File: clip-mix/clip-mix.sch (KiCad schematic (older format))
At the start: 22 parts, among them J1 Conn_01x01_Female, J2 Conn_01x01_Female, J3 Conn_01x01_Female, J4 Conn_02x05_Odd_Even, U1 TL074

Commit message: work on test and clip mix
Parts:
- added unit 4 of U1
- C1, C2: value CP1 -> 10uF
- C3, C4: value C -> 0.1uF
- D1, D2: value D -> 1N4148
- D3: value D_Schottky -> 1N5189
- D4: value D_Schottky -> 1N1589
- J1: value Conn_01x01_Female -> IN
- J2: value Conn_01x01_Female -> OUT
- J3: value Conn_01x01_Female -> CLIP OUT
- J4: value Conn_02x05_Odd_Even -> Power
- R1, R2, R3, R4, R7: value R -> 100K
- R5, R8: value R -> 1K
- R6: value R -> 27K
- RV1: value R_POT -> 20K
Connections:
- net -12V: now reaches D4.1 (K), J4.10 (Pin_10), J4.9 (Pin_9)
- net +12v: now reaches D3.2 (A), J4.1 (Pin_1), J4.2 (Pin_2)
- new net: U1.12 (+), U1.13 (-)
- no-connect marks 0 -> 1
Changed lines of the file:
@@
 P 4400 2450
 F 0 "R2" V 4193 2450 50  0000 C CNN
-F 1 "R" V 4284 2450 50  0000 C CNN
+F 1 "100K" V 4284 2450 50  0000 C CNN
 F 2 "Resistor_THT:R_Axial_DIN0204_L3.6mm_D1.6mm_P7.62mm_Horizontal" V 4330 2450 50  0001 C CNN
 F 3 "~" H 4400 2450 50  0001 C CNN
@@
 P 5100 2000
 F 0 "R3" V 4893 2000 50  0000 C CNN
-F 1 "R" V 4984 2000 50  0000 C CNN
+F 1 "100K" V 4984 2000 50  0000 C CNN
 F 2 "Resistor_THT:R_Axial_DIN0204_L3.6mm_D1.6mm_P7.62mm_Horizontal" V 5030 2000 50  0001 C CNN
 F 3 "~" H 5100 2000 50  0001 C CNN
@@
 P 6600 2550
 F 0 "J2" H 6628 2576 50  0000 L CNN
-F 1 "Conn_01x01_Female" H 6628 2485 50  0000 L CNN
+F 1 "OUT" H 6628 2485 50  0000 L CNN
 F 2 "Connector_Wire:SolderWire-0.5sqmm_1x01_D0.9mm_OD2.3mm" H 6600 2550 50  0001 C CNN
 F 3 "~" H 6600 2550 50  0001 C CNN
@@
 P 7900 3350
 F 0 "J3" H 7928 3376 50  0000 L CNN
-F 1 "Conn_01x01_Female" H 7928 3285 50  0000 L CNN
+F 1 "CLIP OUT" H 7928 3285 50  0000 L CNN
 F 2 "Connector_Wire:SolderWire-0.5sqmm_1x01_D0.9mm_OD2.3mm" H 7900 3350 50  0001 C CNN
 F 3 "~" H 7900 3350 50  0001 C CNN
@@
 P 3750 1900
 F 0 "R1" V 3543 1900 50  0000 C CNN
-F 1 "R" V 3634 1900 50  0000 C CNN
+F 1 "100K" V 3634 1900 50  0000 C CNN
 F 2 "Resistor_THT:R_Axial_DIN0204_L3.6mm_D1.6mm_P7.62mm_Horizontal" V 3680 1900 50  0001 C CNN
 F 3 "~" H 3750 1900 50  0001 C CNN
@@
 P 7350 3350
 F 0 "R8" V 7143 3350 50  0000 C CNN
-F 1 "R" V 7234 3350 50  0000 C CNN
+F 1 "1K" V 7234 3350 50  0000 C CNN
 F 2 "Resistor_THT:R_Axial_DIN0204_L3.6mm_D1.6mm_P7.62mm_Horizontal" V 7280 3350 50  0001 C CNN
 F 3 "~" H 7350 3350 50  0001 C CNN
@@
 P 5950 2550
 F 0 "R5" V 5743 2550 50  0000 C CNN
-F 1 "R" V 5834 2550 50  0000 C CNN
+F 1 "1K" V 5834 2550 50  0000 C CNN
 F 2 "Resistor_THT:R_Axial_DIN0204_L3.6mm_D1.6mm_P7.62mm_Horizontal" V 5880 2550 50  0001 C CNN
 F 3 "~" H 5950 2550 50  0001 C CNN
@@
 P 5500 3250
 F 0 "R4" V 5293 3250 50  0000 C CNN
-F 1 "R" V 5384 3250 50  0000 C CNN
+F 1 "100K" V 5384 3250 50  0000 C CNN
 F 2 "Resistor_THT:R_Axial_DIN0204_L3.6mm_D1.6mm_P7.62mm_Horizontal" V 5430 3250 50  0001 C CNN
 F 3 "~" H 5500 3250 50  0001 C CNN
@@
 P 6000 3550
 F 0 "D2" V 5954 3630 50  0000 L CNN
-F 1 "D" V 6045 3630 50  0000 L CNN
+F 1 "1N4148" V 6045 3630 50  0000 L CNN
 F 2 "Diode_THT:D_T-1_P5.08mm_Horizontal" H 6000 3550 50  0001 C CNN
 F 3 "~" H 6000 3550 50  0001 C CNN
@@
 P 5900 3950
 F 0 "RV1" H 5830 3904 50  0000 R CNN
-F 1 "R_POT" H 5830 3995 50  0000 R CNN
+F 1 "20K" H 5830 3995 50  0000 R CNN
 F 2 "Potentiometer_THT:Potentiometer_Bourns_3296W_Vertical" H 5900 3950 50  0001 C CNN
 F 3 "~" H 5900 3950 50  0001 C CNN
@@
 P 5800 3550
 F 0 "D1" V 5846 3470 50  0000 R CNN
-F 1 "D" V 5755 3470 50  0000 R CNN
+F 1 "1N4148" V 5755 3470 50  0000 R CNN
 F 2 "Diode_THT:D_T-1_P5.08mm_Horizontal" H 5800 3550 50  0001 C CNN
 F 3 "~" H 5800 3550 50  0001 C CNN
@@
 P 6700 3750
 F 0 "R7" V 6493 3750 50  0000 C CNN
-F 1 "R" V 6584 3750 50  0000 C CNN
+F 1 "100K" V 6584 3750 50  0000 C CNN
 F 2 "Resistor_THT:R_Axial_DIN0204_L3.6mm_D1.6mm_P7.62mm_Horizontal" V 6630 3750 50  0001 C CNN
 F 3 "~" H 6700 3750 50  0001 C CNN
@@
 P 6350 3950
 F 0 "R6" H 6280 3904 50  0000 R CNN
-F 1 "R" H 6280 3995 50  0000 R CNN
+F 1 "27K" H 6280 3995 50  0000 R CNN
 F 2 "Resistor_THT:R_Axial_DIN0204_L3.6mm_D1.6mm_P7.62mm_Horizontal" V 6280 3950 50  0001 C CNN
 F 3 "~" H 6350 3950 50  0001 C CNN
@@
 P 2500 2350
 F 0 "J1" H 2392 2125 50  0000 C CNN
-F 1 "Conn_01x01_Female" H 2392 2216 50  0000 C CNN
+F 1 "IN" H 2392 2216 50  0000 C CNN
 F 2 "Connector_Wire:SolderWire-0.5sqmm_1x01_D0.9mm_OD2.3mm" H 2500 2350 50  0001 C CNN
 F 3 "~" H 2500 2350 50  0001 C CNN
@@
 P 3100 5550
 F 0 "C3" H 3215 5596 50  0000 L CNN
-F 1 "C" H 3215 5505 50  0000 L CNN
+F 1 "0.1uF" H 3215 5505 50  0000 L CNN
 F 2 "Capacitor_THT:C_Disc_D7.5mm_W5.0mm_P7.50mm" H 3138 5400 50  0001 C CNN
 F 3 "~" H 3100 5550 50  0001 C CNN
@@
 P 2750 5550
 F 0 "C1" H 2865 5596 50  0000 L CNN
-F 1 "CP1" H 2865 5505 50  0000 L CNN
+F 1 "10uF" H 2865 5505 50  0000 L CNN
 F 2 "Capacitor_THT:CP_Radial_D5.0mm_P2.00mm" H 2750 5550 50  0001 C CNN
 F 3 "~" H 2750 5550 50  0001 C CNN
@@
 P 2300 6250
 F 0 "D4" H 2300 6467 50  0000 C CNN
-F 1 "D_Schottky" H 2300 6376 50  0000 C CNN
+F 1 "1N1589" H 2300 6376 50  0000 C CNN
 F 2 "Diode_THT:D_T-1_P5.08mm_Horizontal" H 2300 6250 50  0001 C CNN
 F 3 "~" H 2300 6250 50  0001 C CNN
@@
 P 2300 5350
 F 0 "D3" H 2300 5133 50  0000 C CNN
-F 1 "D_Schottky" H 2300 5224 50  0000 C CNN
+F 1 "1N5189" H 2300 5224 50  0000 C CNN
 F 2 "Diode_THT:D_T-1_P5.08mm_Horizontal" H 2300 5350 50  0001 C CNN
 F 3 "~" H 2300 5350 50  0001 C CNN
@@
 P 2750 6050
 F 0 "C2" H 2635 6004 50  0000 R CNN
-F 1 "CP1" H 2635 6095 50  0000 R CNN
+F 1 "10uF" H 2635 6095 50  0000 R CNN
 F 2 "Capacitor_THT:CP_Radial_D5.0mm_P2.00mm" H 2750 6050 50  0001 C CNN
 F 3 "~" H 2750 6050 50  0001 C CNN
@@
 P 3100 6050
 F 0 "C4" H 3215 6096 50  0000 L CNN
-F 1 "C" H 3215 6005 50  0000 L CNN
+F 1 "0.1uF" H 3215 6005 50  0000 L CNN
 F 2 "Capacitor_THT:C_Disc_D7.5mm_W5.0mm_P7.50mm" H 3138 5900 50  0001 C CNN
 F 3 "~" H 3100 6050 50  0001 C CNN
@@
 P 1400 5850
 F 0 "J4" H 1450 6267 50  0000 C CNN
-F 1 "Conn_02x05_Odd_Even" H 1450 6176 50  0000 C CNN
+F 1 "Power" H 1450 6176 50  0000 C CNN
 F 2 "Connector_PinHeader_2.54mm:PinHeader_2x05_P2.54mm_Vertical" H 1400 5850 50  0001 C CNN
 F 3 "~" H 1400 5850 50  0001 C CNN
@@
 	5750 4100 5900 4100
 Connection ~ 5900 4100
+$Comp
+L Amplifier_Operational:TL074 U1
+U 4 1 62CC1EBF
+P 8350 2100
+F 0 "U1" H 8350 2467 50  0000 C CNN
+F 1 "TL074" H 8350 2376 50  0000 C CNN
+F 2 "" H 8300 2200 50  0001 C CNN
+F 3 "http://www.ti.com/lit/ds/symlink/tl071.pdf" H 8400 2300 50  0001 C CNN
+	4    8350 2100
+	1    0    0    -1
+$EndComp
+Wire Wire Line
+	8050 2000 8050 2200
+NoConn ~ 8650 2100
+Text GLabel 1200 5650 0    50   Input ~ 0
++12v
+Text GLabel 1200 6050 0    50   Input ~ 0
+-12V
 $EndSCHEMATC

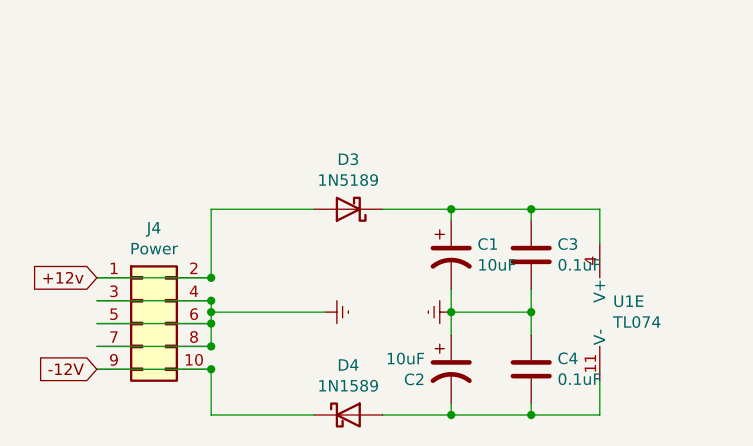
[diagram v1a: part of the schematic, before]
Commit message: start ASREnvelope
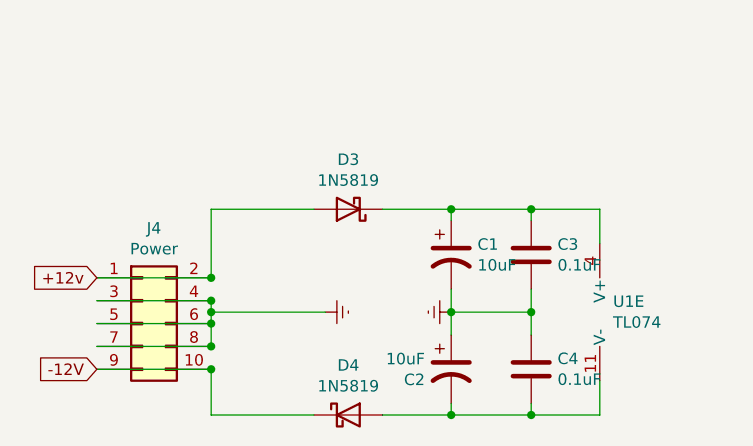
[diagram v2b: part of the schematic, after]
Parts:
- D3: value 1N5189 -> 1N5819
- D4: value 1N1589 -> 1N5819
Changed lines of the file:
@@
 P 2300 6250
 F 0 "D4" H 2300 6467 50  0000 C CNN
-F 1 "1N1589" H 2300 6376 50  0000 C CNN
+F 1 "1N5819" H 2300 6376 50  0000 C CNN
 F 2 "Diode_THT:D_T-1_P5.08mm_Horizontal" H 2300 6250 50  0001 C CNN
 F 3 "~" H 2300 6250 50  0001 C CNN
@@
 P 2300 5350
 F 0 "D3" H 2300 5133 50  0000 C CNN
-F 1 "1N5189" H 2300 5224 50  0000 C CNN
+F 1 "1N5819" H 2300 5224 50  0000 C CNN
 F 2 "Diode_THT:D_T-1_P5.08mm_Horizontal" H 2300 5350 50  0001 C CNN
 F 3 "~" H 2300 5350 50  0001 C CNN
